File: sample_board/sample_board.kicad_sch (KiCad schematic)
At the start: 48 parts, among them J1 Conn_01x10, J2 Conn_01x10, J3 ICSP, J4 USB_B_Micro, U1 ATmega32U4-A, Y1 16MHz

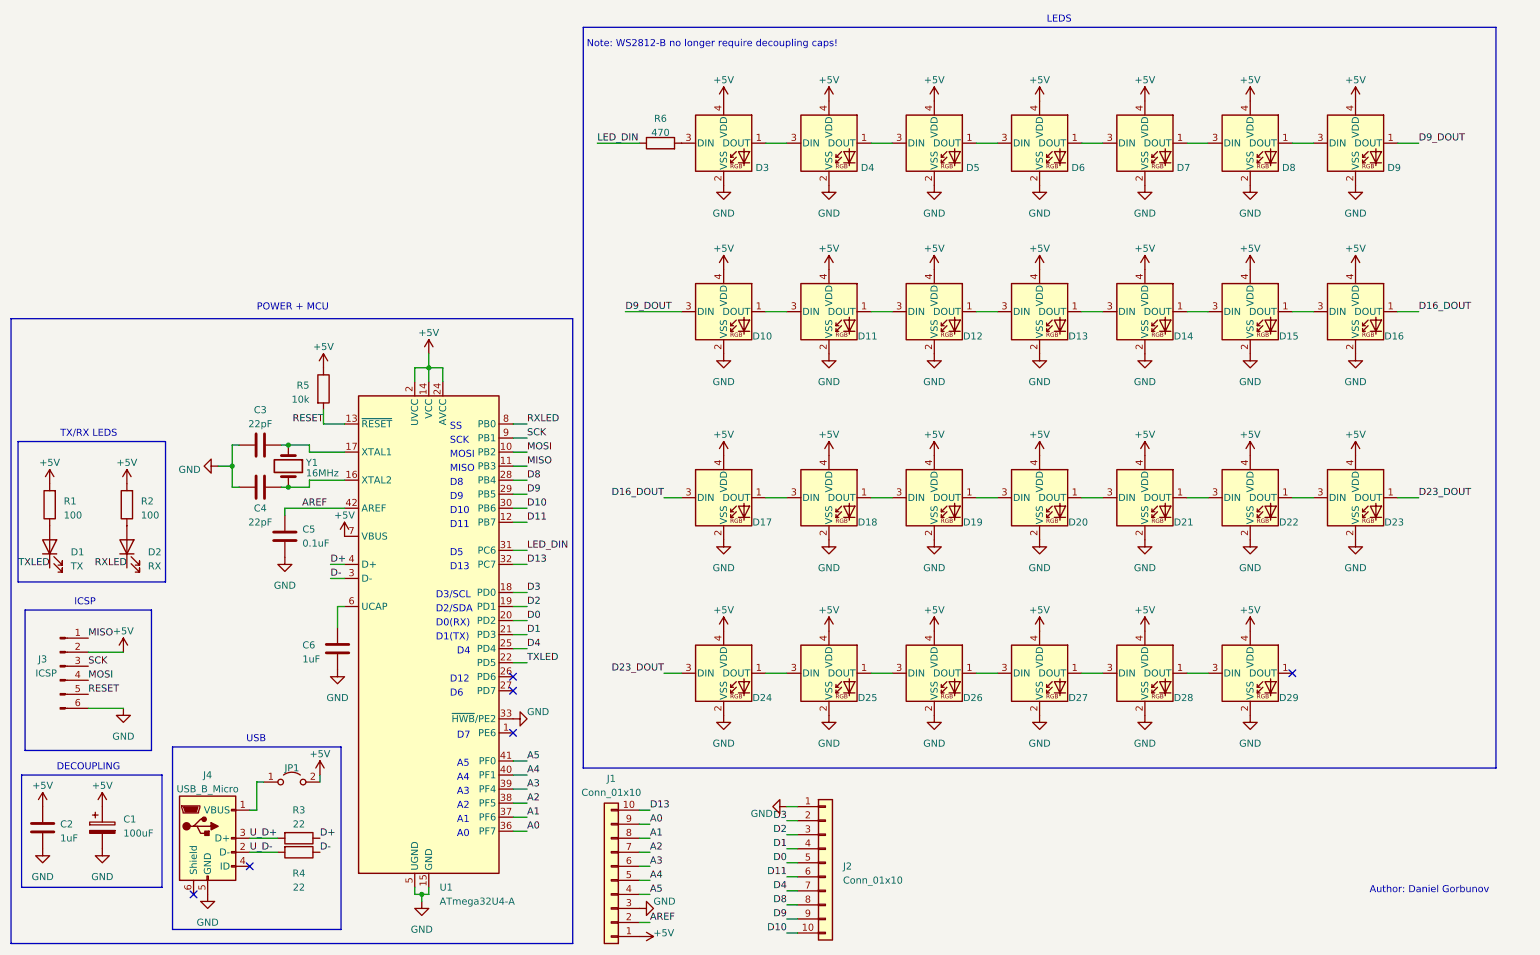
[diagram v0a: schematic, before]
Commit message: sample board rev2; added button
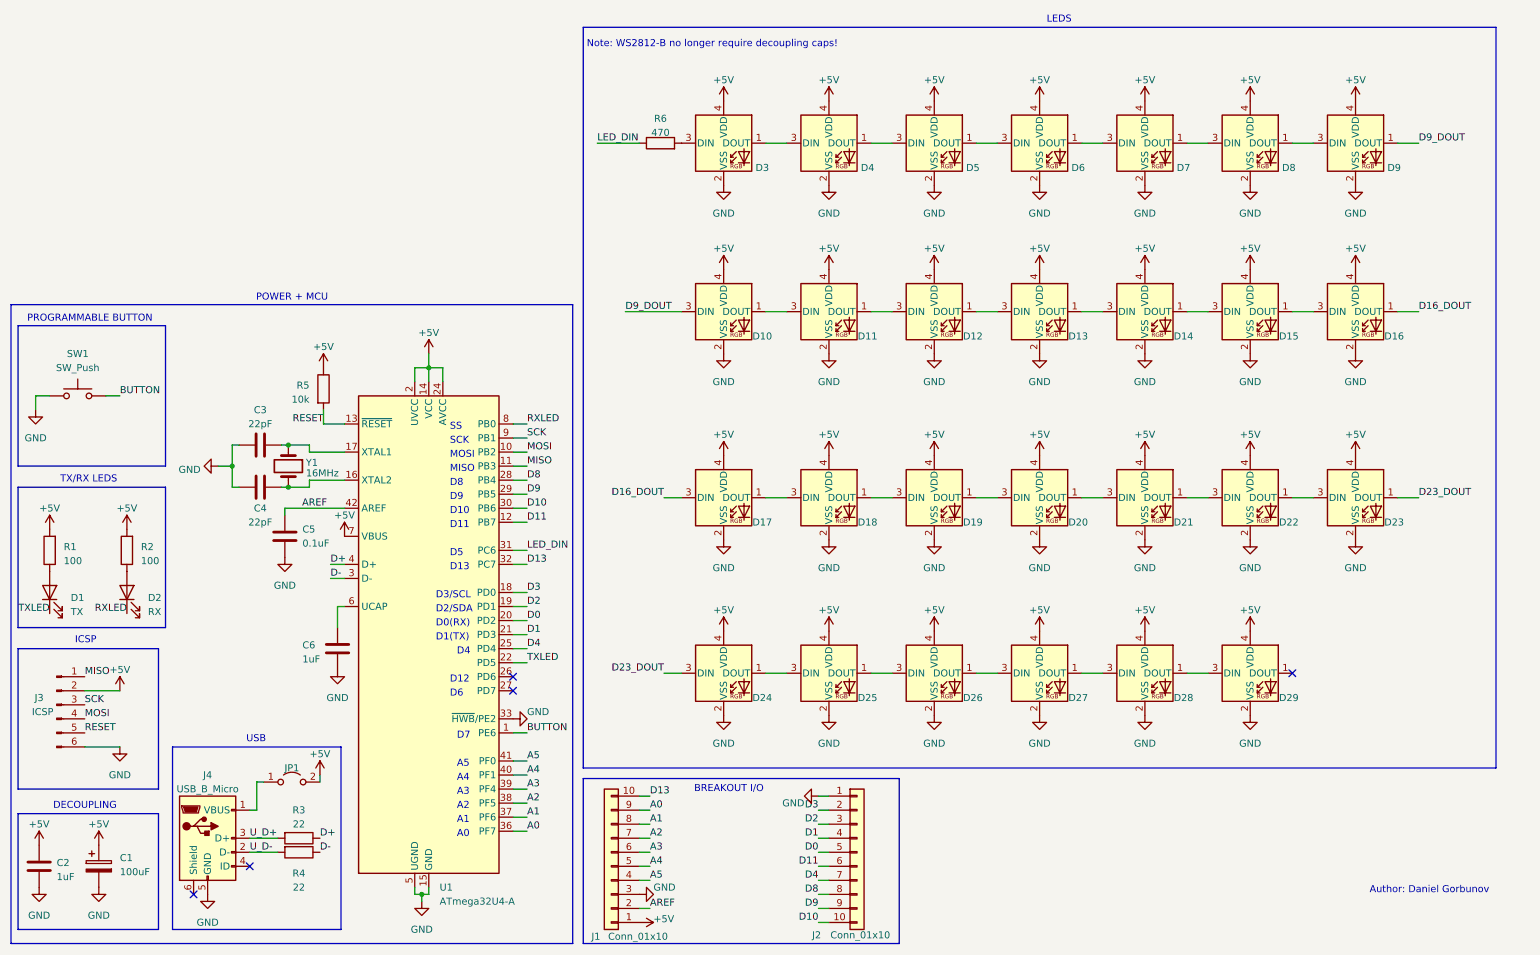
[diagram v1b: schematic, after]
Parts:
- added SW1: SW_Push, Button_Switch_SMD:SW_SPST_PTS647_Sx38, symbol Switch:SW_Push
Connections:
- net GND: now also SW1.1
- net BUTTON: now reaches U1.1 (PE6)
- net BUTTON: now also SW1.2
- no-connect marks 6 -> 5
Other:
- note added: "BREAKOUT I/O"
- note added: "PROGRAMMABLE BUTTON"
- title: Essentials of PCB Design Sample Board -> Essentials of PCB Design Track 1 Board
- moved on the sheet: C1, C2, D1, D2, J1, J2, J3, R1, R2
